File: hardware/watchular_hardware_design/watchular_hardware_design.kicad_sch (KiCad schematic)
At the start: 20 parts, among them U1 ESP32-C3FH4, U2 W25Q16JVSSIQ, Y1 40MHz

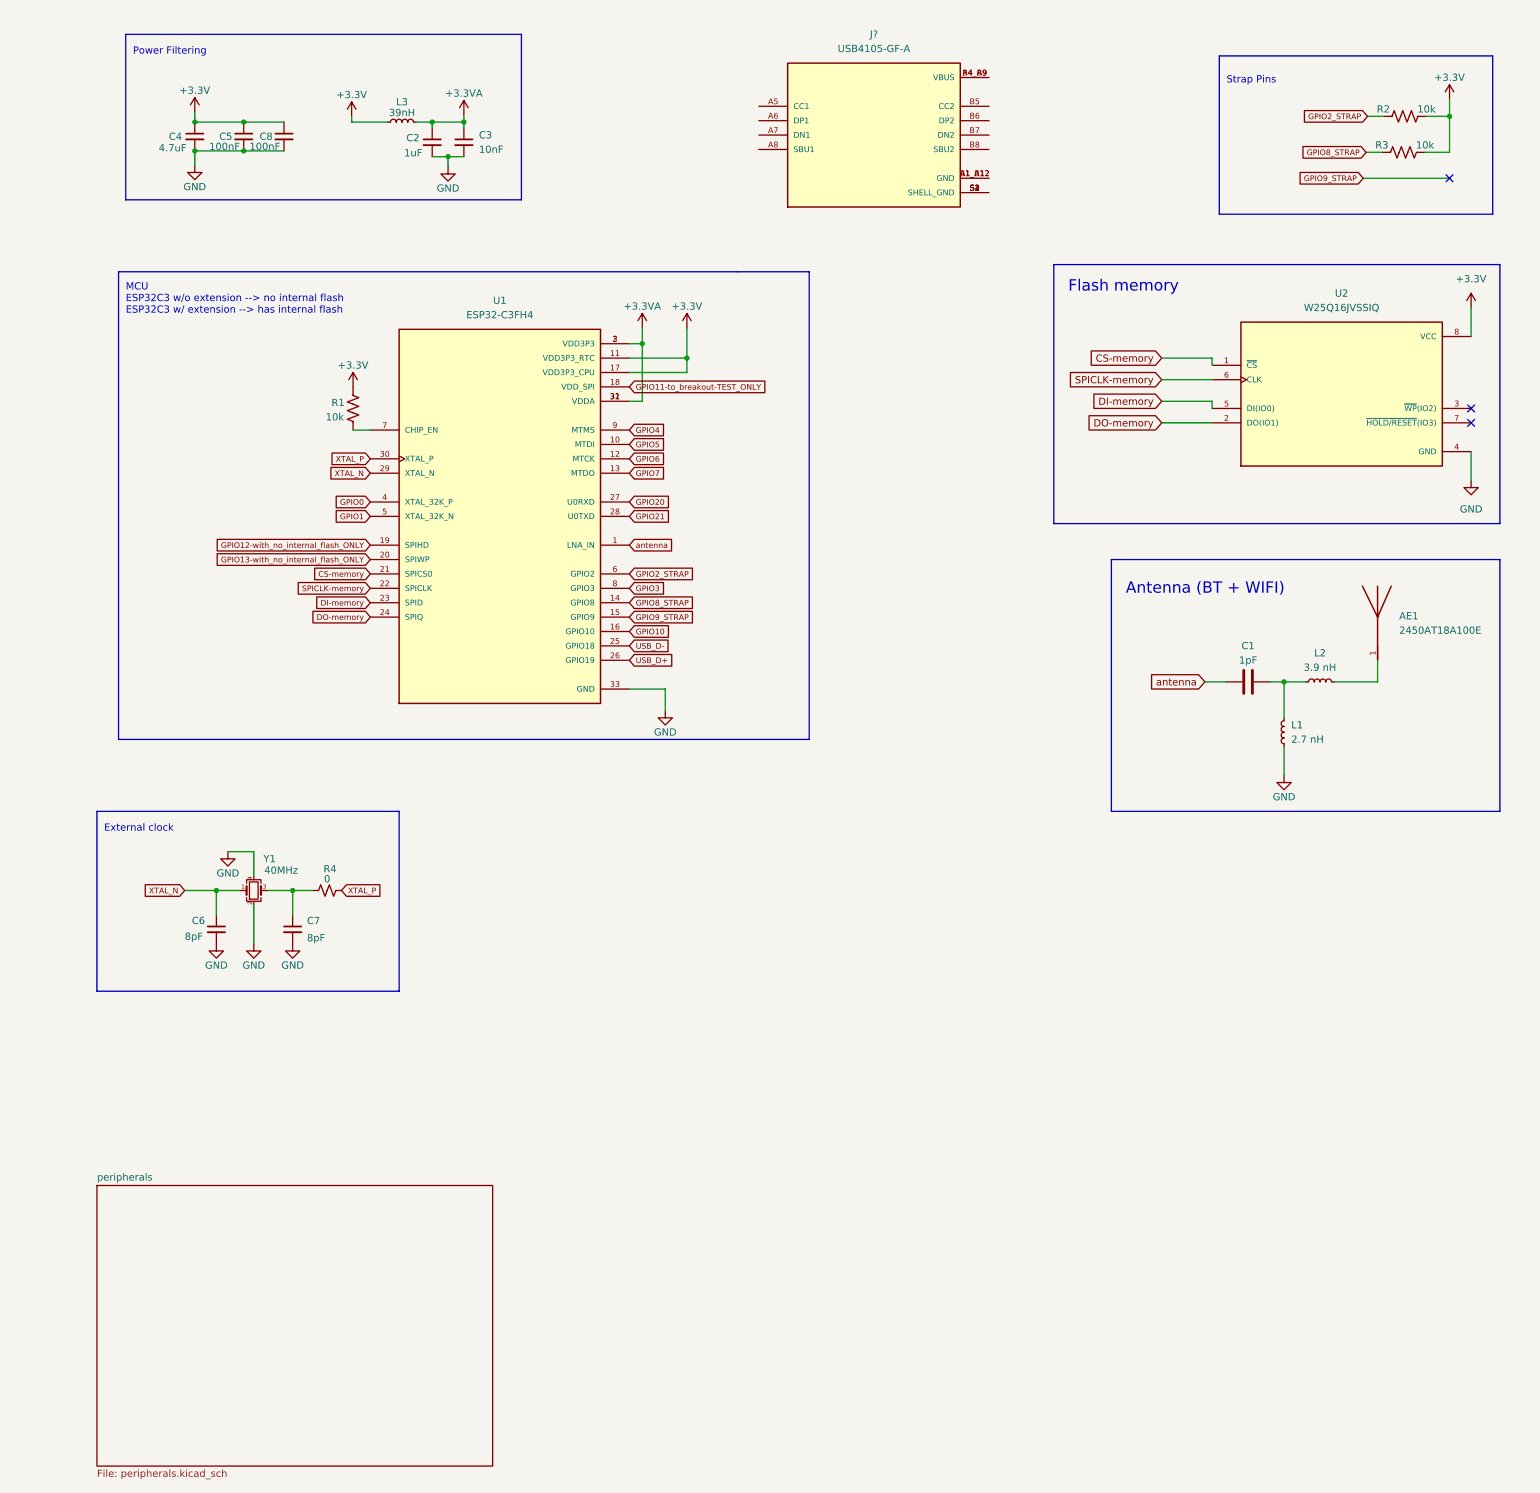
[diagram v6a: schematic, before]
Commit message: Wired up the USB-C
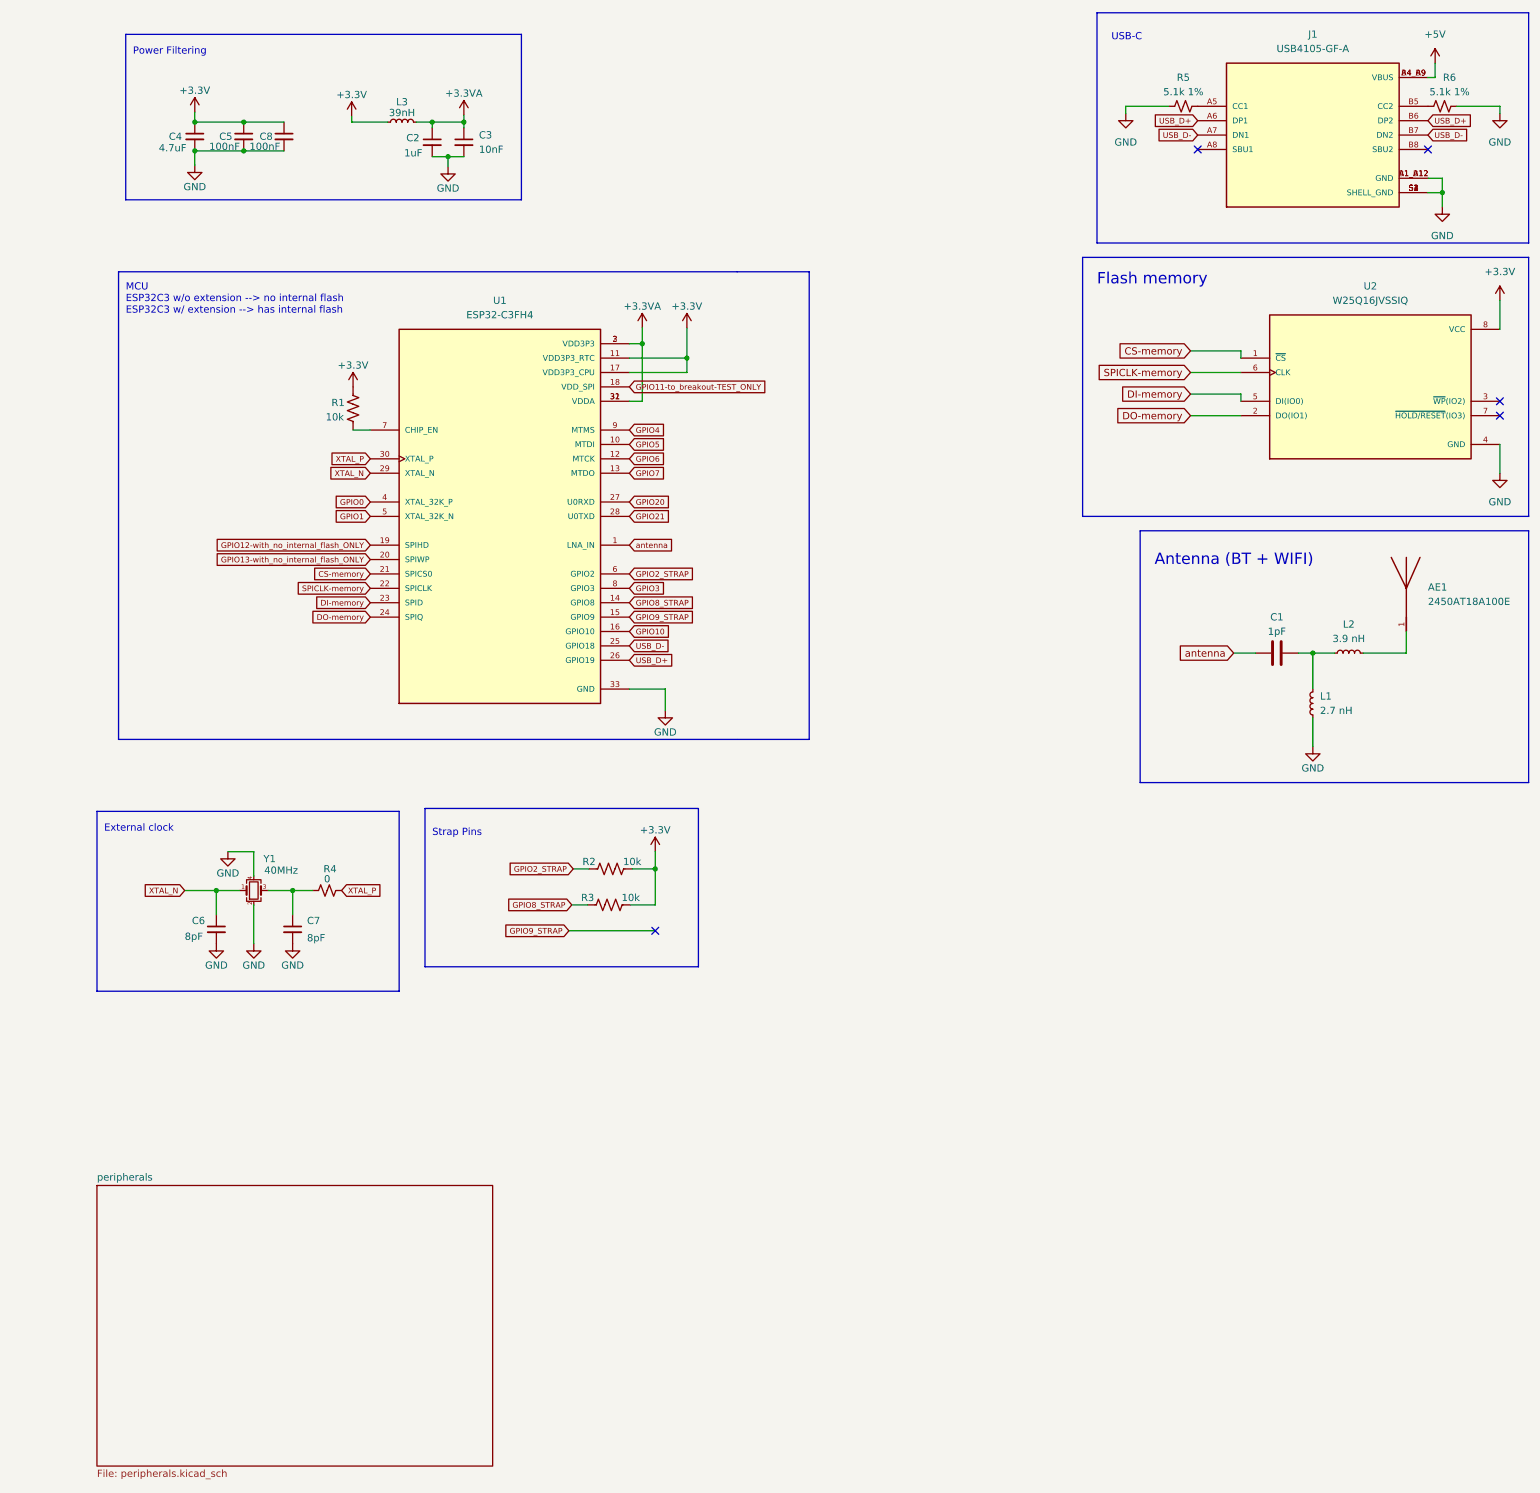
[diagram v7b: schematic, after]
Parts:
- added R5, R6: 5.1k 1%, Resistor_SMD:R_0402_1005Metric_Pad0.72x0.64mm_HandSolder, symbol Device:R_Small_US
- gave numbers to parts that had none: 1
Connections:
- net GND: now also J1.A1_B12 (GND), J1.B1_A12 (GND), J1.S1 (SHELL_GND), J1.S2 (SHELL_GND), J1.S3 (SHELL_GND), J1.S4 (SHELL_GND), R5.1, R6.2
- net USB_D+: now also J1.A6 (DP1), J1.B6 (DP2)
- net USB_D-: now also J1.A7 (DN1), J1.B7 (DN2)
- net +5V: now reaches J1.A4_B9 (VBUS), J1.B4_A9 (VBUS)
- net at J1.A5 (CC1): now also R5.2
- net at J1.B5 (CC2): now also R6.1
- no-connect marks 3 -> 5
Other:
- note added: "USB-C"
- moved on the sheet: AE1, C1, J1, L1, L2, R2, R3, U2

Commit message: Added and wired up the LDO. Boiler plate done.
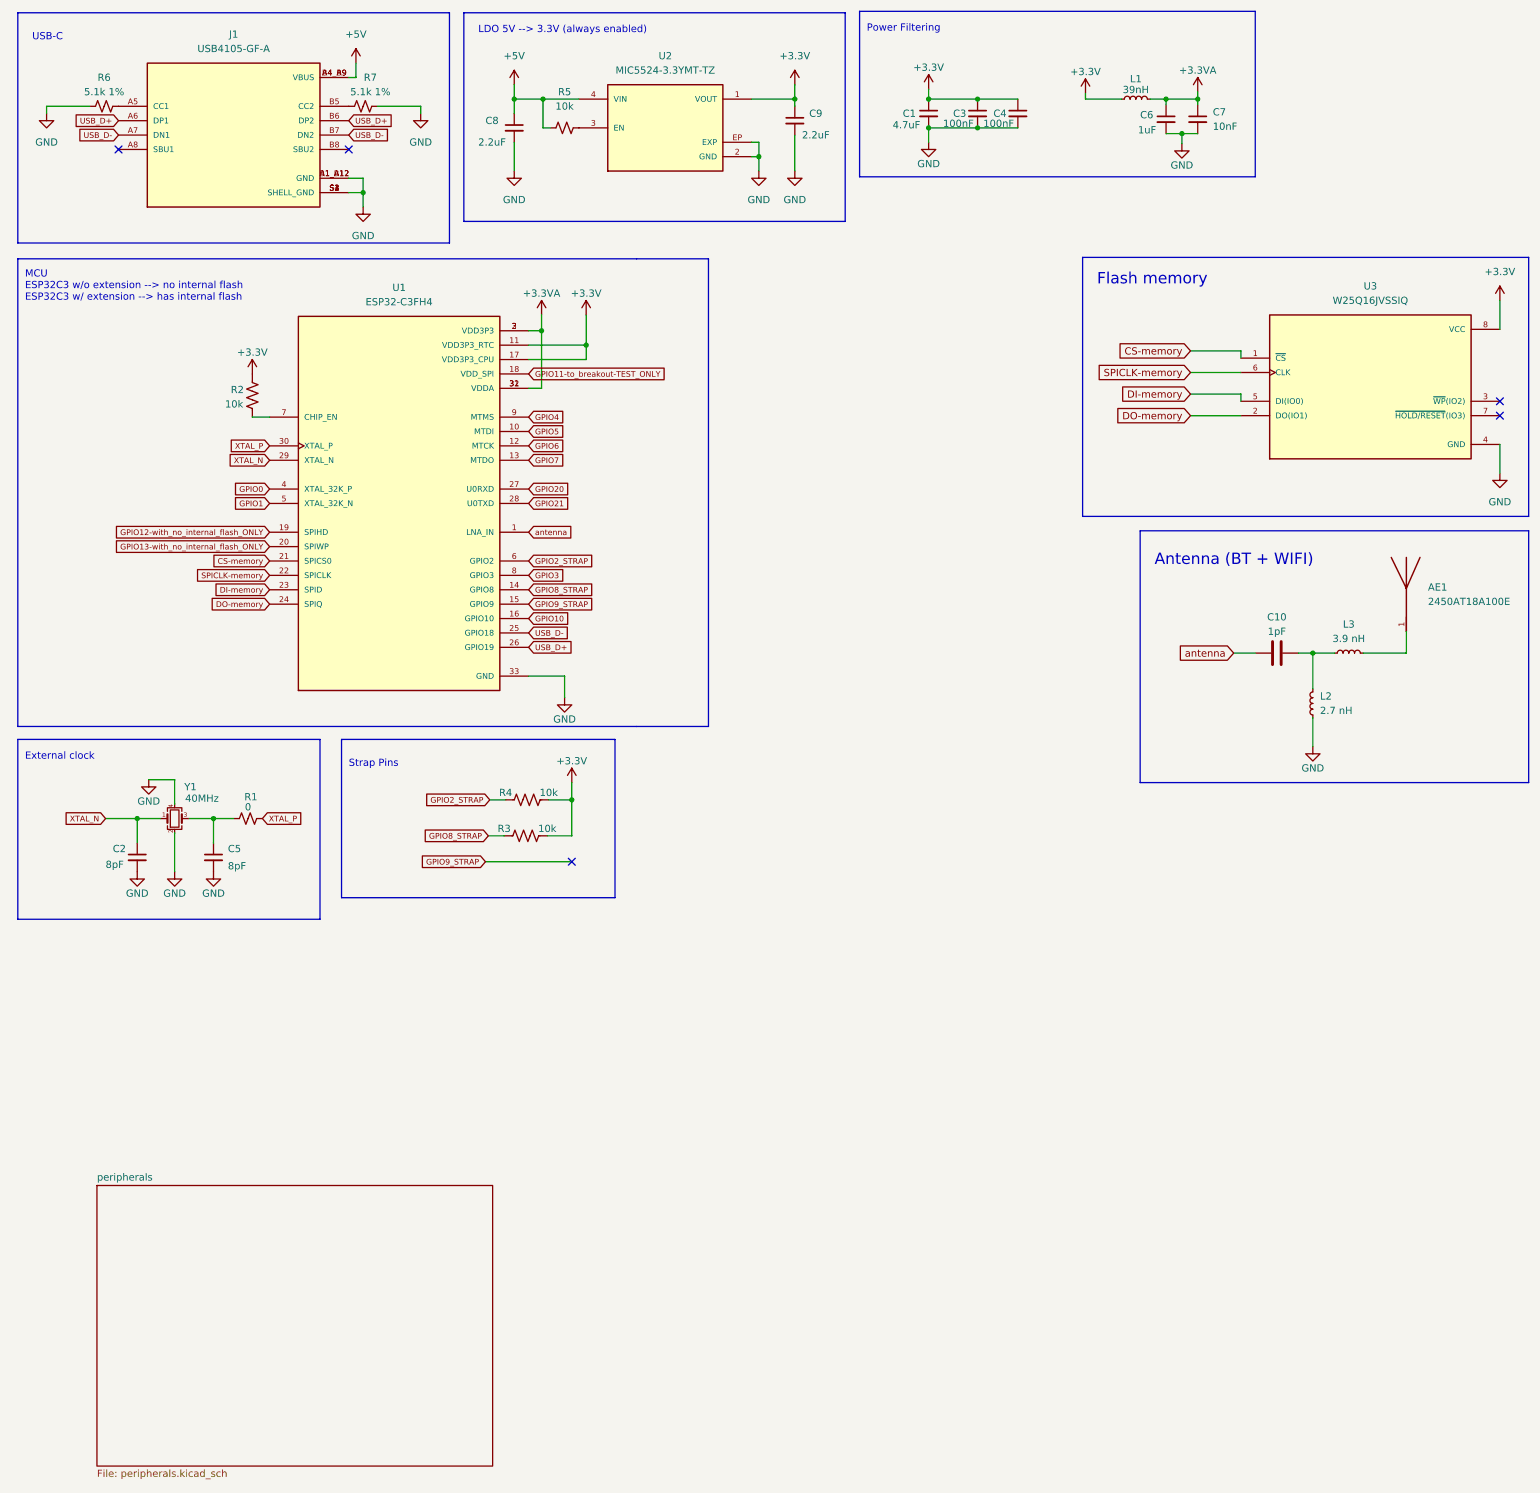
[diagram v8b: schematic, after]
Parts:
- added C8, C9: 2.2uF, Capacitor_SMD:C_0402_1005Metric_Pad0.74x0.62mm_HandSolder, symbol Device:C_Small
- added R5: 10k, Resistor_SMD:R_0402_1005Metric_Pad0.72x0.64mm_HandSolder, symbol Device:R_Small_US
- added U2: MIC5524-3.3YMT-TZ, LDO-MIC5524-3-3YMT-TZ:VREG_MIC5524-3.3YMT-TZ, symbol MIC5524-3.3YMT-TZ:MIC5524-3.3YMT-TZ
- renumbered C4 to C1, C1 to C10, C6 to C2, C5 to C3, C8 to C4, C7 to C5, C2 to C6, C3 to C7, L3 to L1, L1 to L2, L2 to L3, R4 to R1, R1 to R2, R2 to R4, R5 to R6, R6 to R7, U2 to U3
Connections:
- net +3V3: now also C9.1, U2.1 (VOUT)
- net +5V: now also C8.1, R5.1, U2.4 (VIN)
- net GND: now also C8.2, C9.2, U2.2 (GND), U2.EP (EXP)
- new net: R5.2, U2.3 (EN)
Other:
- note added: "LDO 5V --> 3.3V (always enabled)"
- moved on the sheet: C1, C2, C3, C4, C5, C6, C7, J1, L1, R1, R2, R3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
